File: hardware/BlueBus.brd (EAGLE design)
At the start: 90 x 60 mm, 141 parts, among them Q1 NMOSFET-BSS138K, Q2 PMOSFET-DMP32D4S, Q3 NMOSFET-BSS138K, X1 CRYSTAL-12MHZ

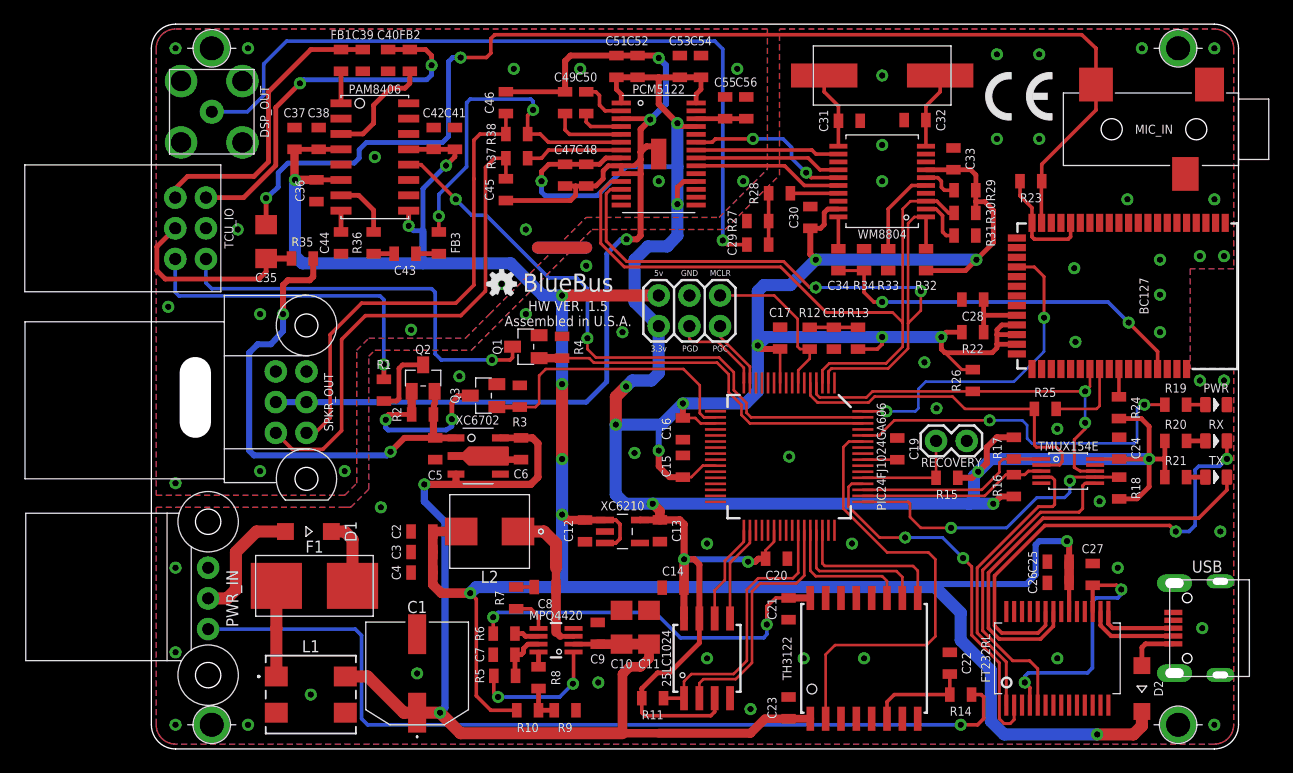
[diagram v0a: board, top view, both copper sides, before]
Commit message: [IMP] hardware: v1.1.6 * Re-wire BC127 power input for use with fixed regulated voltage, rather than battery power
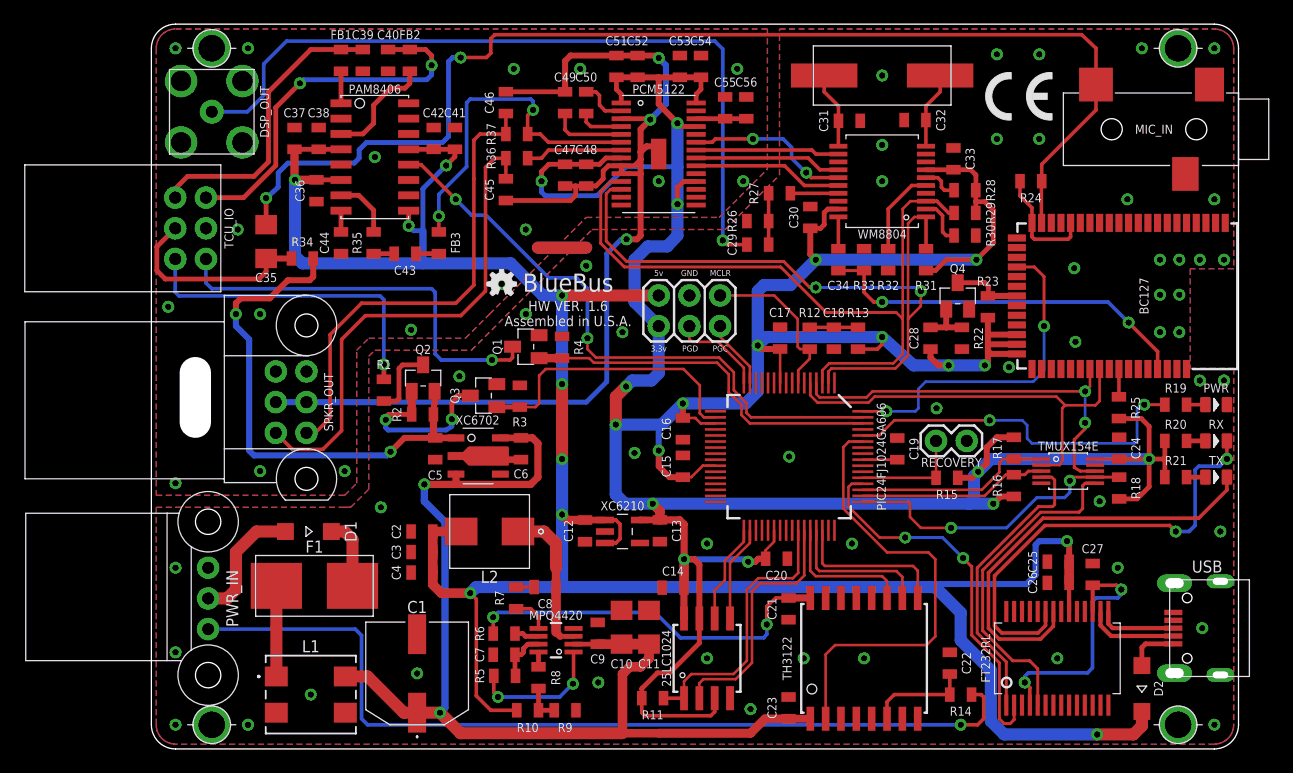
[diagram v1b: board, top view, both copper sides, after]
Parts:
- removed R38: 100, Passives:0805
- added Q4: FDV301N, Passives:SOT-23
- C28: value 4.7uF -> 470NF
- H1, H2, H3, H4: value 2,0-PAD -> 2,2-PAD; device Connectors:2.0-PAD -> Connectors:2.2-PAD
- R22: value 2 -> 100k
- R23: value 2k -> 100k
- R24: value 10k -> 2k
- R26: value 10k -> 110
- R27: value 110 -> 210
- R28: value 210 -> 10k
- R29, R31: value 10k -> 4.7k
- R30, R32: value 4.7k -> 10k
- R33: value 10k -> 75
- R34: value 75 -> 4.7k
- R35: value 4.7k -> 18k
- R36: value 18k -> 100
- moved R34 46.5 mm to (12.5, 40.6), turned to 180 degrees
- moved R26 22.2 mm to (50.2, 43.7), turned to 0 degrees
- moved R24 20.1 mm to (72.8, 47.0), turned to 180 degrees
- moved R28 15.4 mm to (67.3, 46.2), turned to 180 degrees
- moved R36 13.8 mm to (30.2, 48.9), turned to 180 degrees
- moved R23 11.0 mm to (69.2, 36.6), turned to 90 degrees
- moved R25 6.10 mm to (80.1, 28.2), turned to 270 degrees
- moved R35 6.04 mm to (18.4, 41.9), turned to 90 degrees
- moved C28 4.74 mm to (64.5, 34.0), turned to 90 degrees
- moved R31 3.79 mm to (64.1, 40.5), turned to 90 degrees
- moved R32 3.13 mm to (61.0, 40.5)
- moved R27 2.92 mm to (52.0, 46.0)
- moved R33 2.00 mm to (59.0, 40.5), turned to 270 degrees
- moved R37 2.00 mm to (30.2, 50.9)
- moved R29 1.88 mm to (67.3, 44.4)
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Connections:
- removed net 3V3_USB: BC127.34
- removed net BT_3V3_FILTER: BC127.30, C28.1, R22.1
- removed net BT_URX_RES: BC127.42, R25.2
- new net BT_VREGEN: BC127.28, Q4.3, R23.2
- new net BT_VREGEN_CAP_GATE: C28.2, Q4.1, R22.2
- new net VBAT_SENSE: BC127.31
- new net VCHG: BC127.30
- net 12V: now also R34.1; no longer R35.1
- net 3.3V: now also BC127.34, C28.1, R23.1, R25.2, R28.1, R31.1; no longer BC127.31, R22.2, R24.2, R26.2, R30.1, R32.1
- net BT_DOUT: now also R33.2; no longer R34.2
- net BT_MIC_BIAS: now also R24.2; no longer R23.2
- net BT_MIC_L: now also R24.1; no longer R23.1
- net BT_RST: now also R25.1; no longer R24.1
- net BT_URX: now also BC127.42; no longer R25.1
- net BT_UTX: no longer R26.1
- net DAC_OUT_L: now also R37.1; no longer R38.1
- net DAC_OUT_R: now also R36.1; no longer R37.1
- net GND: now also H1.B2.2, H2.B2.2, H3.B2.2, H4.B2.2, Q4.2, R22.1, R26.1, R30.1, R32.1; no longer C28.2, H1.B2,0, H2.B2,0, H3.B2,0, H4.B2,0, R27.1, R31.1, R34.1
- net MCU_SCK3: now also R31.2; no longer R32.2
- net MCU_SDA3: now also R29.2; no longer R30.2
- net SPKR_OUT_L: now also R37.2; no longer R38.2
- net SPKR_OUT_R: now also R36.2; no longer R37.2
- net TEL_AMP_INL: now also R35.2; no longer R36.2
- net TEL_AMP_INL_CAP_RES: now also R35.1; no longer R36.1
- net TEL_MIC_L_OUT: now also R34.2; no longer R35.2
- net WM_CSB: now also R32.2; no longer R33.2
- net WM_GPO0: now also R30.2; no longer R31.2
- net WM_RESETB: now also R28.2; no longer R29.2
- net WM_SPDIF_TX_RES: now also R27.2; no longer R28.2
- net WM_SPDIF_TX_RES2: now also R26.2, R27.1; no longer R27.2, R28.1
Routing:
- net BT_URX_RES: track 6.75 -> 0.00 mm
- net BT_URX: track 28.6 -> 35.2 mm
- net BT_VREGEN: track 0.00 -> 5.87 mm
- net BT_3V3_FILTER: track 5.45 -> 0.00 mm
- net BT_VREGEN_CAP_GATE: track 0.00 -> 4.10 mm
- net 12V: track 41.6 -> 43.3 mm
- net 3.3V: track 320.6 -> 321.7 mm, vias 18 -> 19
- net BT_DATA_IO: track 26.8 -> 27.7 mm
- net GND: vias 66 -> 68
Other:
- board text added: "HW VER. 1.6"
- board text removed: "HW VER. 1.5"

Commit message: [IMP] hardware: v1.6: Minor updates * Re-add 10k resistors to BC127 UART lines * Minor rewiring work around the TMUX154
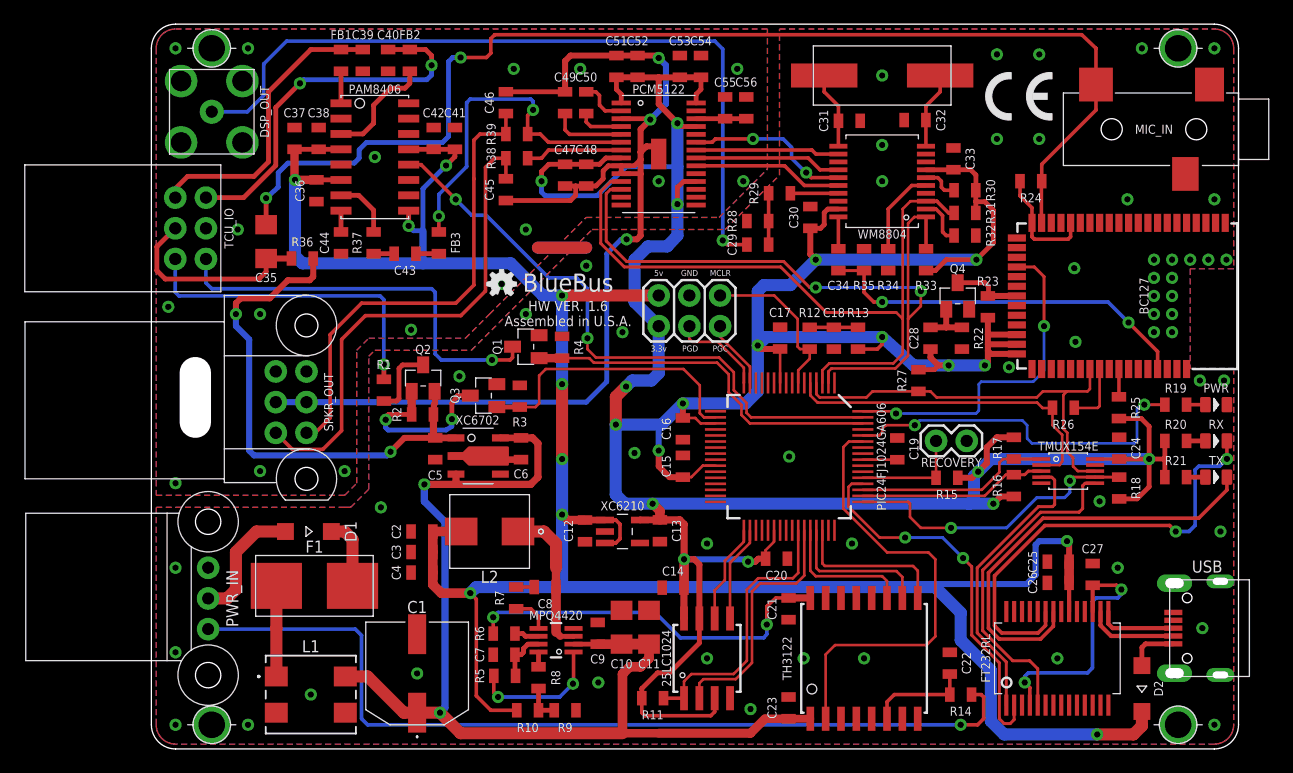
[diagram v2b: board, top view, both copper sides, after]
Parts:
- added R38, R39: 100, Passives:0805
- R26: value 110 -> 10k
- R27: value 210 -> 10k
- R28: value 10k -> 110
- R29: value 4.7k -> 210
- R33: value 75 -> 4.7k
- R34: value 4.7k -> 10k
- R35: value 18k -> 75
- R36: value 100 -> 4.7k
- R37: value 100 -> 18k
- moved R34 48.5 mm to (61.0, 40.5), turned to 90 degrees
- moved R35 40.6 mm to (59.0, 40.5), turned to 270 degrees
- moved R26 29.6 mm to (75.5, 28.2), turned to 180 degrees
- moved R36 19.6 mm to (12.5, 40.6)
- moved R27 19.3 mm to (63.5, 30.5), turned to 90 degrees
- moved R28 17.3 mm to (50.2, 43.7), turned to 0 degrees
- moved R29 15.4 mm to (52.0, 46.0), turned to 0 degrees
- moved R37 14.9 mm to (18.4, 41.9), turned to 90 degrees
- moved R32 6.66 mm to (67.3, 42.5), turned to 180 degrees
- moved R33 5.13 mm to (64.1, 40.5), turned to 90 degrees
- moved R31 5.04 mm to (67.3, 44.4), turned to 180 degrees
- moved R30 3.75 mm to (67.3, 46.2)
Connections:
- new net BT_URX_RES: BC127.42, R26.1
- net 12V: now also R36.1; no longer R34.1
- net 3.3V: now also R27.2, R30.1, R33.1; no longer R28.1, R29.1
- net BT_DOUT: now also R35.2; no longer R33.2
- net BT_URX: now also R26.2; no longer BC127.42
- net BT_UTX: now also R27.1
- net DAC_OUT_L: now also R39.1; no longer R37.1
- net DAC_OUT_R: now also R38.1; no longer R36.1
- net GND: now also R28.1, R34.1, R35.1; no longer R26.1, R30.1, R33.1
- net MCU_SCK3: now also R33.2; no longer R31.2
- net MCU_SDA3: now also R31.2; no longer R29.2
- net SPKR_OUT_L: now also R39.2; no longer R37.2
- net SPKR_OUT_R: now also R38.2; no longer R36.2
- net TEL_AMP_INL: now also R37.2; no longer R35.2
- net TEL_AMP_INL_CAP_RES: now also R37.1; no longer R35.1
- net TEL_MIC_L_OUT: now also R36.2; no longer R34.2
- net WM_CSB: now also R34.2; no longer R32.2
- net WM_GPO0: now also R32.2; no longer R30.2
- net WM_RESETB: now also R30.2; no longer R28.2
- net WM_SPDIF_TX_RES: now also R29.2; no longer R27.2
- net WM_SPDIF_TX_RES2: now also R28.2, R29.1; no longer R26.2, R27.1
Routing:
- net BT_URX: track 35.2 -> 28.2 mm
- net BT_URX_RES: track 0.00 -> 5.24 mm
- net 3.3V: track 321.7 -> 323.5 mm
- net BT_UTX: track 34.0 -> 34.7 mm, vias 2 -> 0
- net BT_DATA_IO: track 27.7 -> 28.2 mm
- net GND: vias 68 -> 72
